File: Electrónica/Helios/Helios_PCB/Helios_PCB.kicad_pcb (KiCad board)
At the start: 2 copper layers, 35 x 30.3 mm, 19 parts, among them J0 Connector J0, J1 Connector J1, Q1 AO3400A, U0 OPA2380, U1 OPA2380

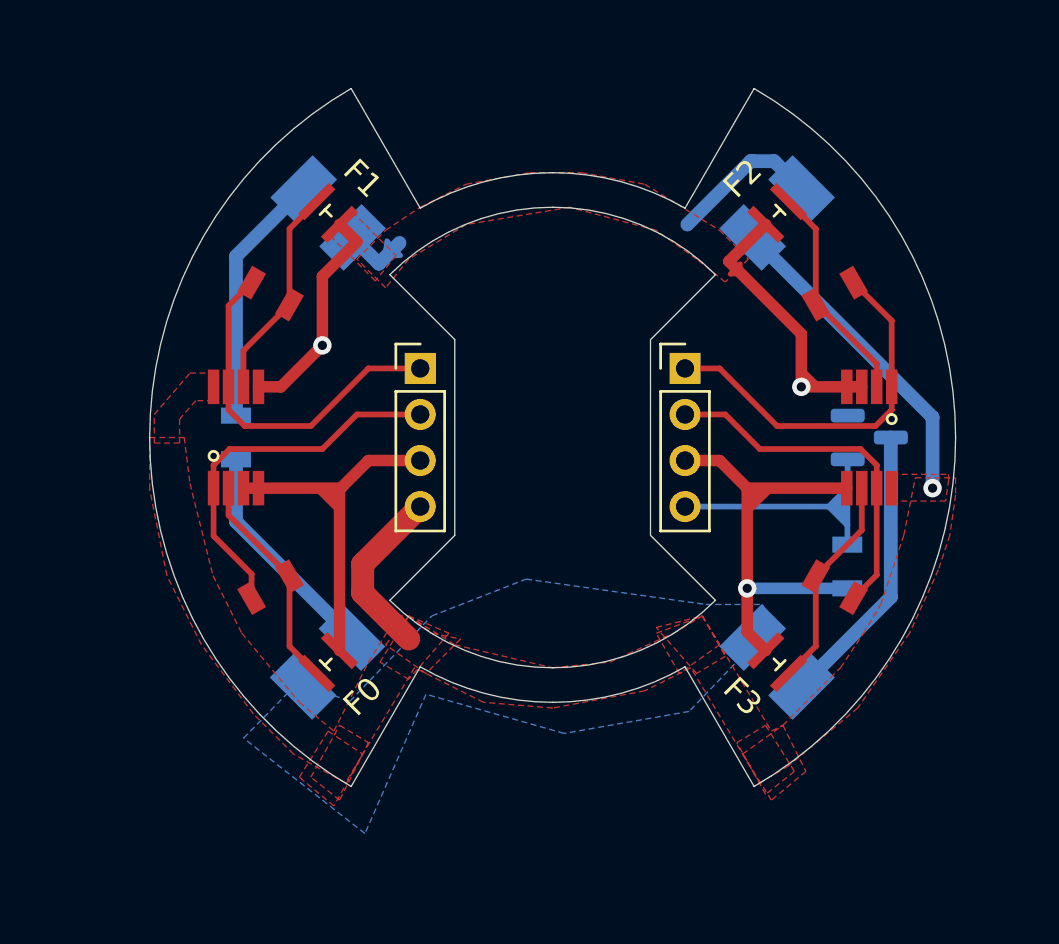
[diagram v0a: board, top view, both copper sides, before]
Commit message: Helios: arreglados errores plano de tierra
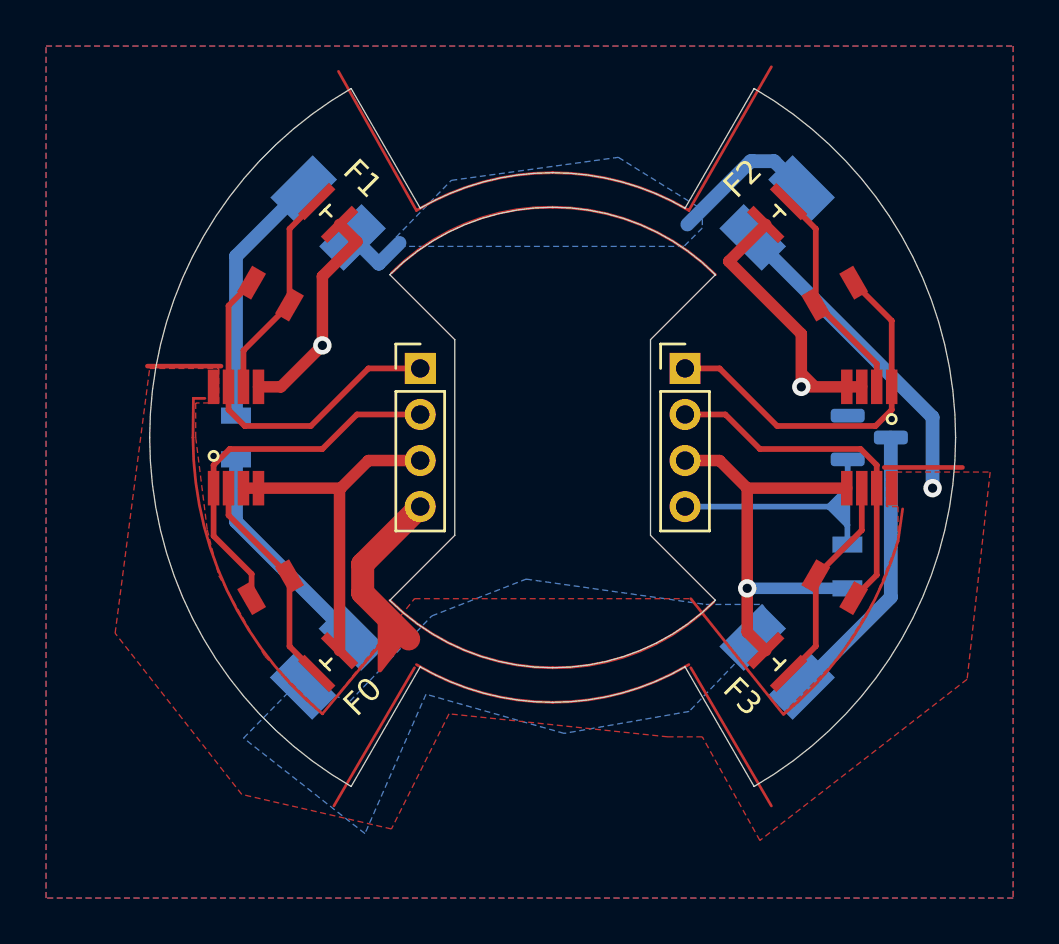
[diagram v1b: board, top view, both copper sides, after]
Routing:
- added copper zone on B.Cu, net GND
- added copper zone on B.Cu, net Net-(D1-Pad2)

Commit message: Helios: Rev 1
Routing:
- net GND: track 57.6 -> 66.2 mm
- removed copper zone on B.Cu, net GND
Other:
- board text added: "07/08/2022"
- board text added: "Helios Module Rev 1"
- board text added: "Jaime Bravo Algaba"
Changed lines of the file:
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@@
       (net 13 "Net-(D1-Pad1)") (pintype "passive"))
   )
-  (gr_line (start 155.916701 90.138831) (end 159.5 83.9) (layer "F.Cu") (width 0.12))
-  (gr_arc (start 157 107.142136) (mid 153.789421 109.279971) (end 150 110) (layer "F.Cu") (width 0.12))
-  (gr_line (start 134.379501 100) (end 134.4 98.3) (layer "F.Cu") (width 0.12))
-  (gr_line (start 160 112) (end 156 107) (layer "F.Cu") (width 0.12))
-  (gr_arc (start 150 110) (mid 146.173166 109.238795) (end 142.928932 107.071068) (layer "F.Cu") (width 0.12))
-  (gr_line (start 144.083299 90.138831) (end 140.7 84.1) (layer "F.Cu") (width 0.12))
-  (gr_arc (start 155.916701 109.861169) (mid 153.069868 111.083198) (end 150 111.5) (layer "F.Cu") (width 0.12))
-  (gr_arc (start 143 92.857864) (mid 146.210579 90.720029) (end 150 90) (layer "F.Cu") (width 0.12))
-  (gr_arc (start 164.999999 104.5) (mid 163.06713 108.631519) (end 160.025582 112.030698) (layer "F.Cu") (width 0.12))
-  (gr_poly
-    (pts
-      (xy 143.6 108.7)
-      (xy 142.5 110.1)
-      (xy 142.5 107.6)
-    ) (layer "F.Cu") (width 0.2) (fill solid))
-  (gr_arc (start 150 90) (mid 153.826834 90.761205) (end 157.071068 92.928932) (layer "F.Cu") (width 0.12))
-  (gr_arc (start 150 111.5) (mid 146.930132 111.083198) (end 144.083299 109.861169) (layer "F.Cu") (width 0.12))
-  (gr_line (start 144 110) (end 140.5 116) (layer "F.Cu") (width 0.12))
-  (gr_line (start 164.4 101.3) (end 167.8 101.3) (layer "F.Cu") (width 0.2))
-  (gr_line (start 140 112) (end 142.5 109) (layer "F.Cu") (width 0.12))
-  (gr_line (start 165 104.5) (end 165.2 103.1) (layer "F.Cu") (width 0.12))
-  (gr_arc (start 140 112) (mid 135.854088 106.625591) (end 134.379501 100) (layer "F.Cu") (width 0.12))
-  (gr_arc (start 144.083299 90.138831) (mid 146.930132 88.916802) (end 150 88.5) (layer "F.Cu") (width 0.12))
-  (gr_line (start 134.4 98.3) (end 134.9 98.3) (layer "F.Cu") (width 0.12))
-  (gr_poly
-    (pts
-      (xy 161.6 97.8)
-      (xy 160.8 97.8)
-      (xy 160.8 97)
-    ) (layer "F.Cu") (width 0.2) (fill solid))
-  (gr_line (start 135.6 96.9) (end 132.4 96.9) (layer "F.Cu") (width 0.2))
-  (gr_arc (start 150 88.5) (mid 153.069868 88.916802) (end 155.916701 90.138831) (layer "F.Cu") (width 0.12))
-  (gr_line (start 159.5 116) (end 156 110) (layer "F.Cu") (width 0.12))
   (gr_poly
     (pts
@@
   (gr_line (start 150 100) (end 142.5 107.5) (layer "Dwgs.User") (width 0.15))
   (gr_line (start 150 100) (end 143 93) (layer "Dwgs.User") (width 0.15))
+  (gr_line (start 155.916701 90.138831) (end 159.5 83.9) (layer "Dwgs.User") (width 0.12))
+  (gr_arc (start 157 107.142136) (mid 153.789421 109.279971) (end 150 110) (layer "Dwgs.User") (width 0.12))
   (gr_circle (center 150 100) (end 160 100) (layer "Dwgs.User") (width 0.15) (fill none))
+  (gr_line (start 134.379501 100) (end 134.4 98.3) (layer "Dwgs.User") (width 0.12))
+  (gr_line (start 160 112) (end 156 107) (layer "Dwgs.User") (width 0.12))
+  (gr_arc (start 150 110) (mid 146.173166 109.238795) (end 142.928932 107.071068) (layer "Dwgs.User") (width 0.12))
   (gr_arc (start 160.237588 114.193019) (mid 134.421043 92.028419) (end 167.5 100) (layer "Dwgs.User") (width 0.15))
   (gr_circle (center 150 100) (end 158 100) (layer "Dwgs.User") (width 0.15) (fill none))
+  (gr_line (start 144.083299 90.138831) (end 140.7 84.1) (layer "Dwgs.User") (width 0.12))
+  (gr_arc (start 155.916701 109.861169) (mid 153.069868 111.083198) (end 150 111.5) (layer "Dwgs.User") (width 0.12))
   (gr_circle (center 150 100) (end 167.5 100) (layer "Dwgs.User") (width 0.15) (fill none))
   (gr_line (start 150 100) (end 157.5 107.5) (layer "Dwgs.User") (width 0.15))
+  (gr_arc (start 143 92.857864) (mid 146.210579 90.720029) (end 150 90) (layer "Dwgs.User") (width 0.12))
+  (gr_arc (start 164.999999 104.5) (mid 163.06713 108.631519) (end 160.025582 112.030698) (layer "Dwgs.User") (width 0.12))
+  (gr_arc (start 150 90) (mid 153.826834 90.761205) (end 157.071068 92.928932) (layer "Dwgs.User") (width 0.12))
   (gr_line (start 150 100) (end 141 115.25) (layer "Dwgs.User") (width 0.15))
+  (gr_arc (start 150 111.5) (mid 146.930132 111.083198) (end 144.083299 109.861169) (layer "Dwgs.User") (width 0.12))
+  (gr_line (start 144 110) (end 140.5 116) (layer "Dwgs.User") (width 0.12))
+  (gr_line (start 164.4 101.3) (end 167.8 101.3) (layer "Dwgs.User") (width 0.2))
   (gr_line (start 150 100) (end 157 93) (layer "Dwgs.User") (width 0.15))
+  (gr_line (start 140 112) (end 142.7 108.7) (layer "Dwgs.User") (width 0.12))
+  (gr_line (start 165 104.5) (end 165.2 103.1) (layer "Dwgs.User") (width 0.12))
+  (gr_arc (start 140 112) (mid 135.854088 106.625591) (end 134.379501 100) (layer "Dwgs.User") (width 0.12))
+  (gr_arc (start 144.083299 90.138831) (mid 146.930132 88.916802) (end 150 88.5) (layer "Dwgs.User") (width 0.12))
+  (gr_line (start 134.4 98.3) (end 134.9 98.3) (layer "Dwgs.User") (width 0.12))
+  (gr_line (start 135.6 96.9) (end 132.4 96.9) (layer "Dwgs.User") (width 0.2))
+  (gr_arc (start 150 88.5) (mid 153.069868 88.916802) (end 155.916701 90.138831) (layer "Dwgs.User") (width 0.12))
+  (gr_line (start 159.5 116) (end 156 110) (layer "Dwgs.User") (width 0.12))
   (gr_circle (center 150 100) (end 163.75 100) (layer "Dwgs.User") (width 0.15) (fill none))
   (gr_line (start 154.25 95.75) (end 157.071068 92.928932) (layer "Edge.Cuts") (width 0.05))
@@
   (gr_arc (start 132.5 100) (mid 134.844555 91.25) (end 141.25 84.844555) (layer "Edge.Cuts") (width 0.05))
   (gr_arc (start 150 88.5) (mid 152.976419 88.891853) (end 155.75 90.040708) (layer "Edge.Cuts") (width 0.05))
+  (gr_text "07/08/2022" (at 157.6 100 270) (layer "B.SilkS")
+    (effects (font (size 0.5 0.5) (thickness 0.125)) (justify mirror))
+  )
+  (gr_text "Helios Module Rev 1" (at 157.5 100 270) (layer "F.SilkS")
+    (effects (font (size 0.5 0.5) (thickness 0.0625)))
+  )
+  (gr_text "Jaime Bravo Algaba" (at 142.5 99.8 90) (layer "F.SilkS")
+    (effects (font (size 0.5 0.5) (thickness 0.0625)))
+  )
   (segment (start 158.45 102.2) (end 157.25 101) (width 0.5) (layer "F.Cu") (net 1))
   (segment (start 159.255025 90.744975) (end 157.65 92.35) (width 0.5) (layer "F.Cu") (net 1))
@@
   (segment (start 137.225 102.2) (end 140.8 102.2) (width 0.5) (layer "F.Cu") (net 1))
   (segment (start 159.255025 109.255025) (end 158.45 108.45) (width 0.5) (layer "F.Cu") (net 1))
-  (segment (start 140.744975 109.255025) (end 140.744975 102.255025) (width 0.5) (layer "F.Cu") (net 1))
   (segment (start 141.5 91.5) (end 140.744975 90.744975) (width 0.5) (layer "F.Cu") (net 1))
   (segment (start 162.775 102.2) (end 158.45 102.2) (width 0.5) (layer "F.Cu") (net 1))
@@
   (via (at 158.45 106.55) (size 0.8) (drill 0.4) (layers "F.Cu" "B.Cu") (net 1))
   (via (at 160.8 97.8) (size 0.8) (drill 0.4) (layers "F.Cu" "B.Cu") (net 1))
+  (segment (start 144.25 101) (end 140 96.75) (width 0.6) (layer "B.Cu") (net 1))
+  (segment (start 157.6 101) (end 160.8 97.8) (width 0.5) (layer "B.Cu") (net 1))
+  (segment (start 140 96.75) (end 140 96) (width 0.6) (layer "B.Cu") (net 1))
   (segment (start 162.8 106.55) (end 158.45 106.55) (width 0.5) (layer "B.Cu") (net 1))
+  (segment (start 162.8125 99.05) (end 161.5625 97.8) (width 0.5) (layer "B.Cu") (net 1))
+  (segment (start 161.5625 97.8) (end 160.8 97.8) (width 0.5) (layer "B.Cu") (net 1))
+  (segment (start 155.75 101) (end 157.6 101) (width 0.5) (layer "B.Cu") (net 1))
   (segment (start 138.572724 106.025) (end 135.925 103.377276) (width 0.25) (layer "F.Cu") (net 2))
   (segment (start 139.744975 110.244975) (end 138.572724 109.072724) (width 0.25) (layer "F.Cu") (net 2))
@@
   (segment (start 142.45 92.45) (end 143.35 91.55) (width 0.6) (layer "B.Cu") (net 12))
   (segment (start 159.62132 88) (end 158.7 88) (width 0.6) (layer "B.Cu") (net 12))
-  (segment (start 158.6 88) (end 155.85 90.75) (width 0.6) (layer "B.Cu") (net 12))
+  (segment (start 158.6 88) (end 155.6 91) (width 0.6) (layer "B.Cu") (net 12))
   (segment (start 141.31066 91.31066) (end 142.45 92.45) (width 0.6) (layer "B.Cu") (net 12))
   (segment (start 136.25 92.12868) (end 136.25 99.05) (width 0.6) (layer "B.Cu") (net 13))
@@
     )
   )
-  (zone (net 1) (net_name "GND") (layer "B.Cu") (hatch edge 0.508)
-    (connect_pads (clearance 0.254))
-    (min_thickness 0.254) (filled_areas_thickness no)
-    (fill yes (thermal_gap 0.508) (thermal_bridge_width 0.508))
-    (polygon
-      (pts
-        (xy 170 120)
-        (xy 128 120)
-        (xy 128 83)
-        (xy 170 83)
+  (zone (net 0) (net_name "") (layer "B.Cu") (hatch edge 0.508)
+    (connect_pads (clearance 0))
+    (min_thickness 0.254)
+    (keepout (tracks not_allowed) (vias not_allowed) (pads not_allowed) (copperpour not_allowed) (footprints allowed))
+    (fill (thermal_gap 0.508) (thermal_bridge_width 0.508))
+    (polygon
+      (pts
+        (xy 161.7 85.8)
+        (xy 161.4 86.4)
+        (xy 160.4 87.6)
+        (xy 160 87.7)
+        (xy 159.7 87.6)
+        (xy 158.4 87.6)
+        (xy 155.8 90.1)
+        (xy 158.6 84.7)
       )
     )
@@
         (xy 152.851668 87.832676)
         (xy 156.5 90.1)
-        (xy 156.5 90.9)
-        (xy 155.7 91.7)
+        (xy 156.3 90.7)
+        (xy 155.5 91.5)
         (xy 143.2 91.7)
         (xy 143.2 91.3)
@@
     (connect_pads (clearance 0.2))
     (min_thickness 0.254) (filled_areas_thickness no)
-    (fill yes (thermal_gap 0.508) (thermal_bridge_width 0.508) (island_removal_mode 1) (island_area_min 0))
-    (polygon
-      (pts
+    (fill yes (thermal_gap 0.508) (thermal_bridge_width 0.508))
+    (polygon
+      (pts
